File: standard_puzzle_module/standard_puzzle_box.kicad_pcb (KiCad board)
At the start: 2 copper layers, 76 parts, among them U1 ESP32-C3-DevKitM-1

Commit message: feat: salvaging stuff after lossy crash
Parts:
- R_BO1, R_BO2, R_BO3, R_BO4, R_BO5, R_BO6, R_SIN1, R_SIN2, R_SIN3, R_SIN4, R_SO1, R_SO10, R_SO2, R_SO3, R_SO4, R_SO5, R_SO6, R_SO7, R_SO8, R_SO9: footprint Resistor_THT:R_Axial_DIN0411_L9.9mm_D3.6mm_P15.24mm_Horizontal -> Resistor_THT:R_Axial_DIN0207_L6.3mm_D2.5mm_P10.16mm_Horizontal
- U1: value ESP32-C3-DevKitM-1 -> ESP32-C3-SuperMini; footprint RF_Module:ESP32-C3-DevKitM-1 -> ESP32-C3-SuperMini:ESP32-C3-SuperMini
- moved R_BO6 204.4 mm to (106.4, 87.4)
- moved J_BI4 197.0 mm to (172.0, 32.2), turned to 180 degrees
- moved J_BI3 190.6 mm to (188.6, 31.8), turned to 180 degrees
- moved CP_BO2 188.4 mm to (153.9, 106.0)
- moved R_BO4 187.1 mm to (139.2, 86.6)
- moved R_BO5 184.8 mm to (131.7, 93.8), turned to -90 degrees
- moved D_BO2 183.9 mm to (153.8, 98.5), turned to 180 degrees
- moved J_BO2 183.1 mm to (146.9, 106.0), turned to 180 degrees
- moved CP_BO1 181.5 mm to (184.1, 105.7)
- moved U_BO2 181.4 mm to (165.2, 88.6), turned to 180 degrees
- moved Q_BO2 179.6 mm to (146.2, 91.5), turned to 180 degrees
- moved D_BI3 179.6 mm to (191.0, 50.1), turned to 180 degrees
- moved D_BI4 179.5 mm to (177.5, 50.1), turned to 180 degrees
- moved U_BI4 177.8 mm to (174.0, 56.6), turned to 180 degrees
- moved CC_BO2 177.5 mm to (158.8, 92.9), turned to 180 degrees
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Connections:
- CC_PI1 pad 1: Net-(DCREG1-Vin) -> +12V
- CP_PI1 pad 1: Net-(DCREG1-Vin) -> +12V
- DCREG1 pad 1: Net-(DCREG1-Vin) -> +12V
- D_SCHP1 pad 1: Net-(DCREG1-Vin) -> +12V
- FUSE1 pad 1: +12V -> Net-(J_PWR1-Pin_1)
- J_PWR1 pad 1: +12V -> Net-(J_PWR1-Pin_1)
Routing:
- net +12V: track 8.02 -> 97.5 mm
- net GND: track 57.0 -> 93.4 mm, vias 8 -> 14
- net +5V: track 43.5 -> 10.6 mm
- net +3.3V: track 29.4 -> 0.00 mm, vias 0 -> 1
- net Net-(DCREG1-Vin): track 19.7 -> 0.00 mm
- net Net-(D_BO3-A): track 0.00 -> 15.9 mm
- net Net-(D_BO1-A): track 0.00 -> 15.9 mm
- net Net-(D_BO2-A): track 0.00 -> 15.2 mm
- net Net-(Q_BO3-G): track 0.00 -> 14.2 mm
- net Net-(Q_BO2-G): track 0.00 -> 13.7 mm
- net Net-(R_BO5-Pad1): track 0.00 -> 13.7 mm, vias 0 -> 2
- net /signal_input/out: track 13.3 -> 0.00 mm
- net Net-(R_BO3-Pad1): track 0.00 -> 11.9 mm, vias 0 -> 2
- net Net-(Q_BO1-G): track 0.00 -> 11.7 mm
- net Net-(R_BO1-Pad1): track 0.00 -> 11.6 mm, vias 0 -> 2
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
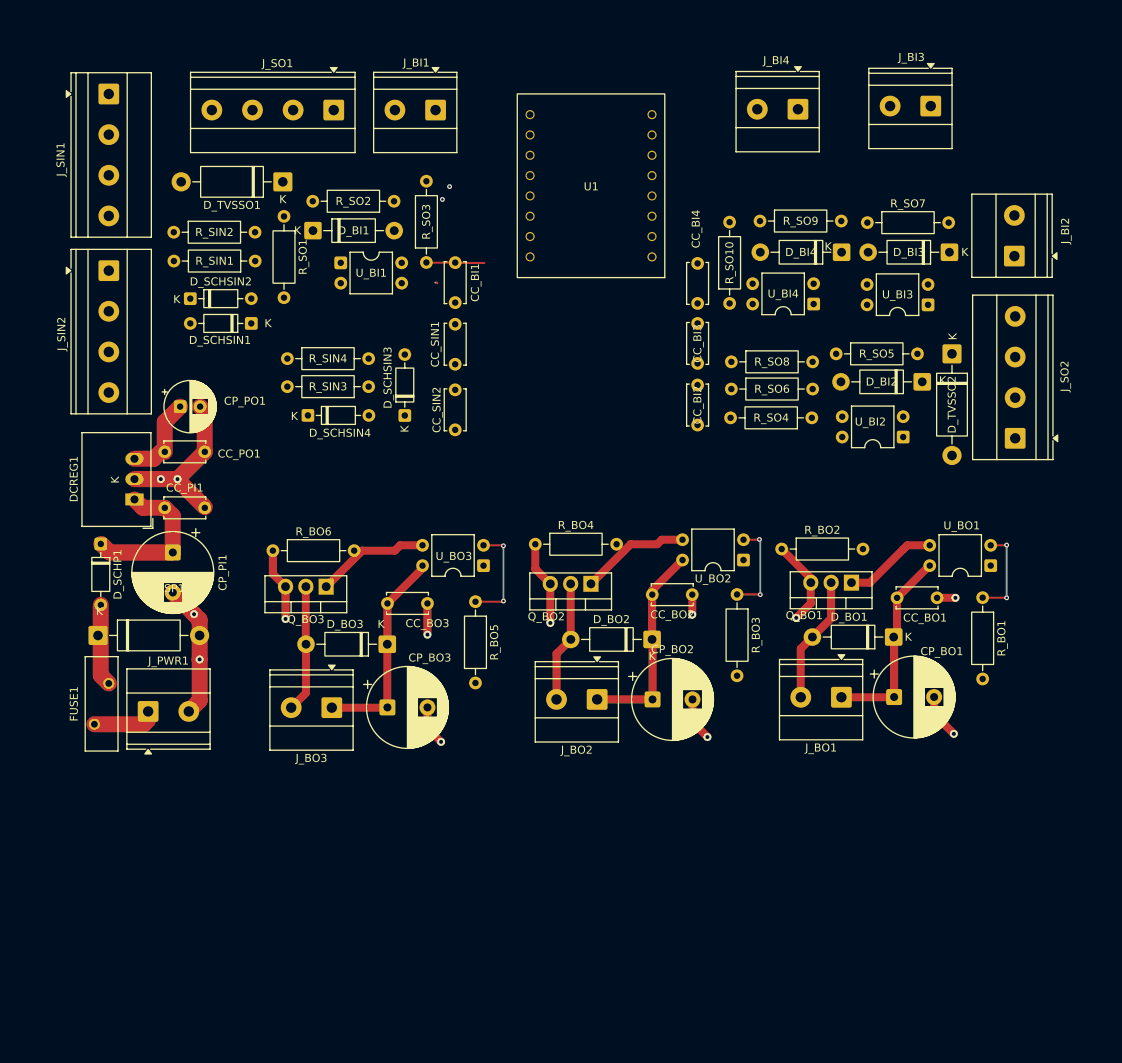
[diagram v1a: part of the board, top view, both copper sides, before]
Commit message: feat: improve component placement for pcb
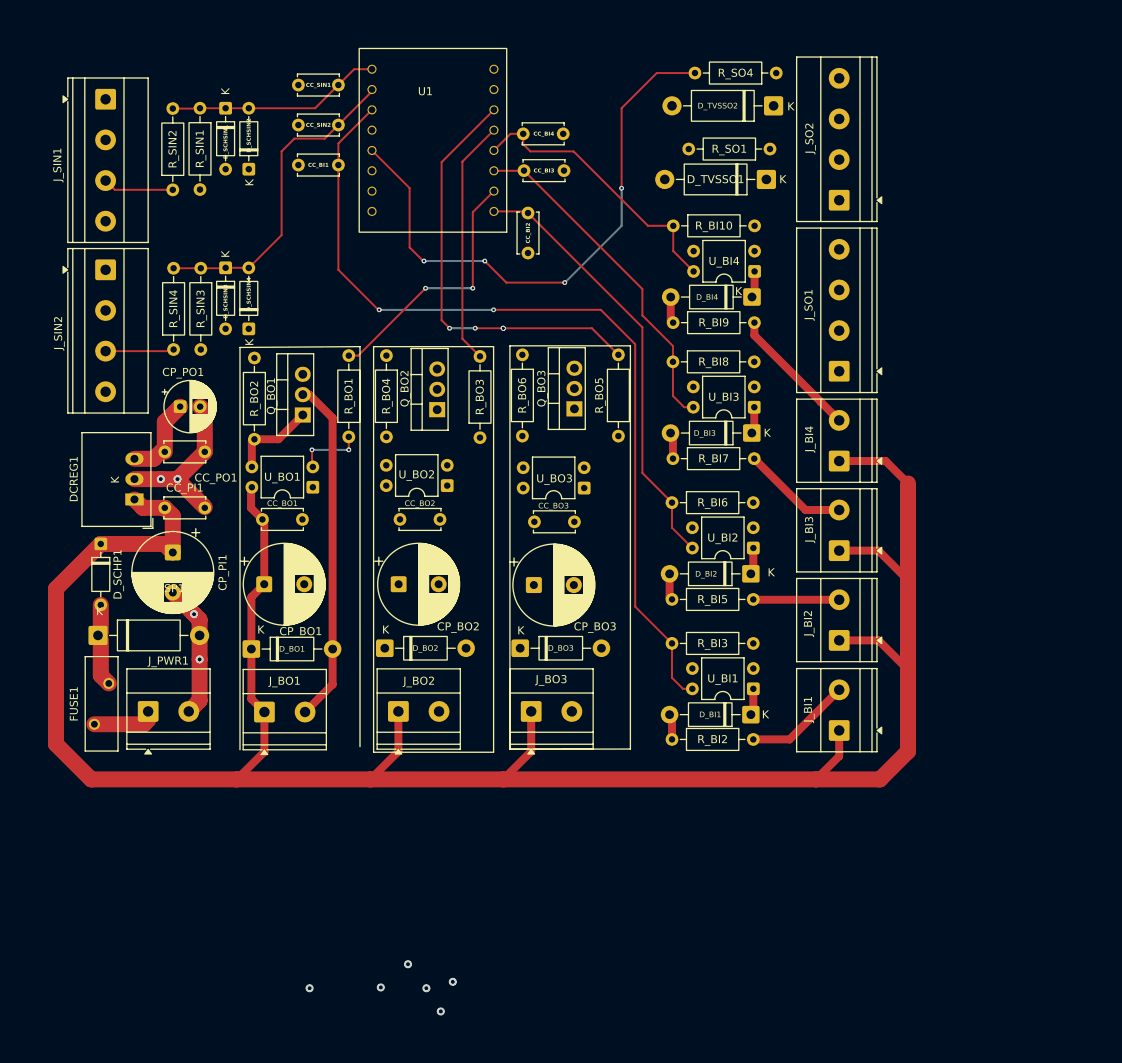
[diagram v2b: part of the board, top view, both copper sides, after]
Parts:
- moved J_BI1 92.5 mm to (177.2, 109.9), turned to 90 degrees
- moved U_BO1 85.3 mm to (111.4, 79.5)
- moved R_BO1 81.7 mm to (115.9, 73.2), turned to 90 degrees
- moved D_BI1 81.6 mm to (166.2, 107.9), turned to 180 degrees
- moved D_BO1 80.3 mm to (103.7, 99.7), turned to 0 degrees
- moved CP_BO1 80.0 mm to (105.3, 91.6)
- moved CC_BO1 79.9 mm to (110.1, 83.5)
- moved R_BI2 75.7 mm to (156.3, 111.0), turned to 0 degrees
- moved U_BI1 74.1 mm to (166.5, 104.7), turned to 180 degrees
- moved J_BO1 72.1 mm to (105.4, 107.6), turned to 0 degrees
- moved Q_BO1 71.7 mm to (110.2, 70.4), turned to 90 degrees
- moved J_SO1 71.1 mm to (177.2, 65.0), turned to 90 degrees
- moved R_BO2 70.1 mm to (104.1, 63.3), turned to -90 degrees
- moved R_SO1 61.3 mm to (168.6, 37.2), turned to 180 degrees
- moved D_TVSSO1 60.5 mm to (168.1, 41.0)
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- renumbered R_SO10 to R_BI10, R_SO2 to R_BI2, R_SO3 to R_BI3, R_SO5 to R_BI5, R_SO6 to R_BI6, R_SO7 to R_BI7, R_SO8 to R_BI8, R_SO9 to R_BI9
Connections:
- U1 pad 0: GND -> /signal_input/out
- U1 pad 1: GND -> /signal_input1/out
- U1 pad 10: /signal_input1/out -> /boolean_output2/in
- U1 pad 2: +3.3V -> /boolean_input/out
- U1 pad 20: /signal_output1/in -> unconnected-(U1-GPIO20-Pad20)
- U1 pad 21: /boolean_input1/out -> unconnected-(U1-GPIO21-Pad21)
- U1 pad 3: +3.3V -> /signal_output/in
- U1 pad 3V3: +5V -> (no net)
- U1 pad 4: /boolean_input/out -> /signal_output1/in
- U1 pad 5: /signal_output/in -> /boolean_input1/out
- U1 pad 5V: +5V -> (no net)
- U1 pad 6: GND -> /boolean_output/in
- U1 pad 7: unconnected-(U1-RST-Pad7) -> /boolean_input2/out
- U1 pad 8: GND -> /boolean_input3/out
- U1 pad 9: /signal_input/out -> /boolean_output1/in
- U1 pad GND: /boolean_output2/in -> (no net)
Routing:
- net +12V: track 97.5 -> 287.7 mm
- net /boolean_input/out: track 7.26 -> 109.3 mm, vias 0 -> 2
- net /signal_output1/in: track 0.00 -> 71.0 mm, vias 0 -> 4
- net GND: track 93.4 -> 38.2 mm, vias 14 -> 10
- net /boolean_input1/out: track 0.00 -> 54.7 mm
- net /boolean_output2/in: track 0.00 -> 53.0 mm, vias 0 -> 6
- net /boolean_input2/out: track 0.00 -> 42.8 mm
- net /signal_input1/out: track 0.00 -> 40.3 mm
- net /boolean_input3/out: track 0.00 -> 35.6 mm
- net /boolean_output/in: track 0.00 -> 32.1 mm, vias 0 -> 2
- net /boolean_output1/in: track 0.00 -> 30.8 mm
- net Net-(D_BO1-A): track 15.9 -> 43.1 mm
- net /signal_input/out: track 0.00 -> 26.9 mm
- net Net-(J_BI4-Pin_2): track 0.00 -> 16.6 mm
- net Net-(D_BO3-A): track 15.9 -> 0.00 mm
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
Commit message: feat: DRC approved prototype of the board
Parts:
- moved CC_BO3 33.4 mm to (110.7, 84.8)
- moved CP_BO3 33.4 mm to (105.6, 91.9)
- moved D_BO3 33.4 mm to (103.9, 99.8)
- moved J_BO3 33.4 mm to (105.3, 107.7)
- moved Q_BO3 33.4 mm to (110.7, 69.9)
- moved R_BO5 33.4 mm to (116.2, 73.3)
- moved U_BO3 33.4 mm to (111.9, 79.8)
- moved R_BO6 33.3 mm to (104.3, 63.1)
- moved J_BO1 30.6 mm to (136.0, 107.7)
- moved CP_BO1 30.6 mm to (135.9, 91.7)
- moved U_BO1 30.6 mm to (142.0, 79.6)
- moved CC_BO1 30.6 mm to (140.7, 83.6)
- moved D_BO1 30.6 mm to (134.3, 99.8)
- moved Q_BO1 30.6 mm to (140.8, 70.5)
- moved R_BO1 30.6 mm to (146.5, 73.3)
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- renumbered D_SCHSIN1 to DS_SI1, D_SCHSIN2 to DS_SI2, D_SCHSIN3 to DS_SI3, D_SCHSIN4 to DS_SI4
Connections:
- U1 pad 3V3: (no net) -> +3.3V
- U1 pad 5V: (no net) -> +5V
- U1 pad GND: (no net) -> GND
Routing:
- net +3.3V: track 0.00 -> 289.4 mm, vias 0 -> 23
- net +5V: track 10.6 -> 224.4 mm
- net /signal_output/in: track 0.00 -> 67.2 mm, vias 0 -> 2
- net +12V: track 287.7 -> 349.0 mm
- net Net-(D_BO3-A): track 0.00 -> 46.8 mm
- net Net-(D_BO2-A): track 0.00 -> 46.6 mm
- net Net-(D_TVSSO1-K): track 0.00 -> 25.9 mm, vias 0 -> 2
- net Net-(D_TVSSO2-K): track 0.00 -> 15.0 mm
- net Net-(Q_BO3-G): track 0.00 -> 11.8 mm
- net Net-(Q_BO2-G): track 0.00 -> 11.3 mm
- net /boolean_input1/out: track 54.7 -> 64.0 mm, vias 0 -> 4
- net /boolean_output/in: track 32.1 -> 40.5 mm
- net /boolean_input2/out: track 42.8 -> 50.4 mm, vias 0 -> 4
- net Net-(R_BO5-Pad1): track 0.00 -> 7.26 mm
- net Net-(R_BO3-Pad1): track 0.00 -> 6.66 mm
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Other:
- board outline added: 112 x 95 mm

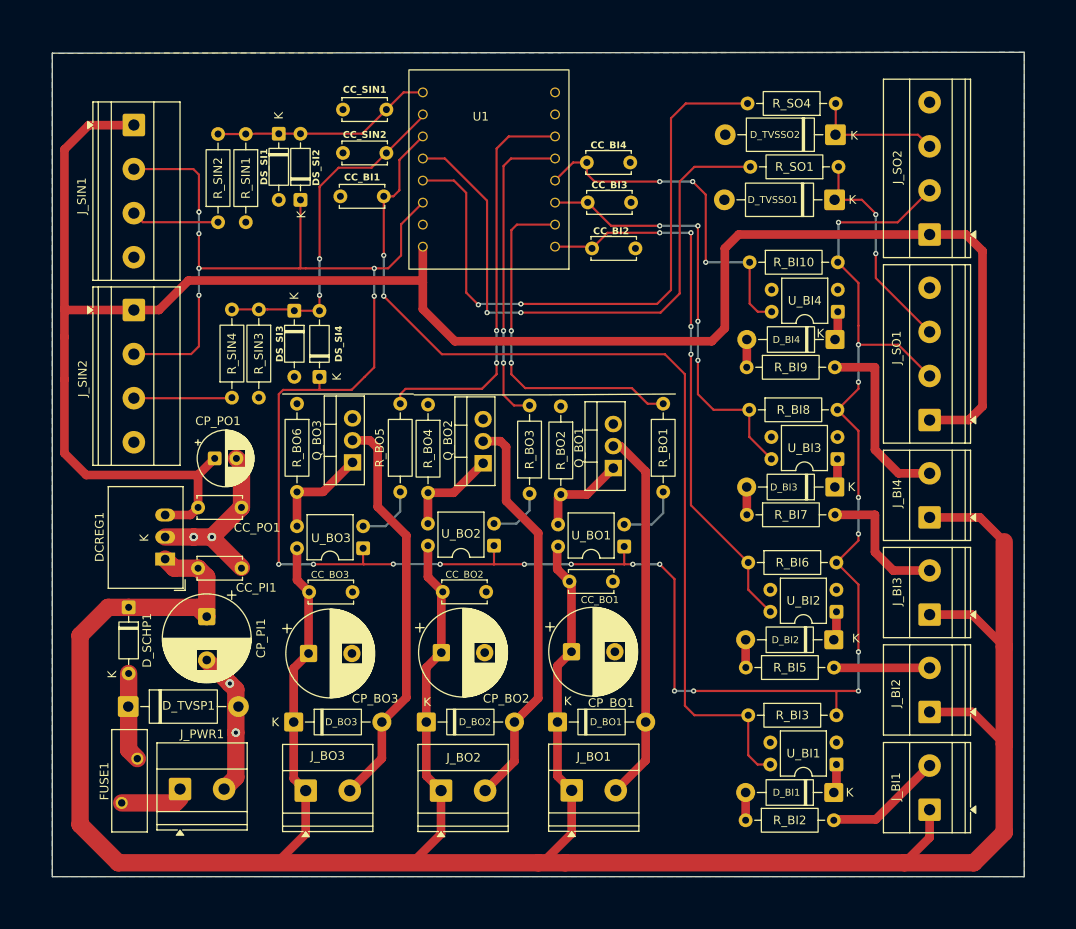
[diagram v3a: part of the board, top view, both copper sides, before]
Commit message: feat: decrease the board size
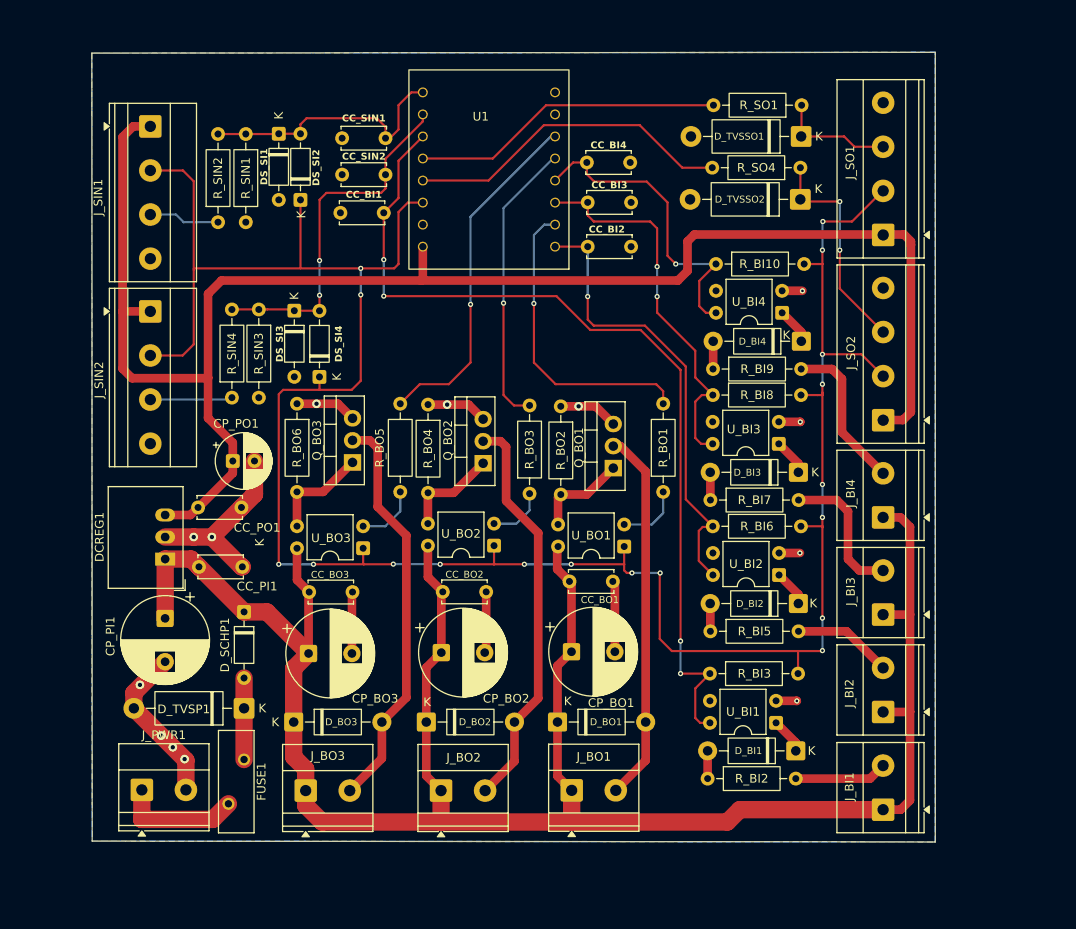
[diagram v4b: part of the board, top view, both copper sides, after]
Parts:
- moved J_SO2 22.1 mm to (171.8, 65.0)
- moved J_SO1 22.0 mm to (171.8, 43.6)
- moved D_TVSP1 13.4 mm to (98.2, 98.2), turned to 180 degrees
- moved D_SCHP1 13.3 mm to (98.2, 87.1)
- moved FUSE1 12.3 mm to (96.4, 109.2)
- moved D_TVSSO2 8.48 mm to (162.3, 39.5)
- moved U_BI1 8.45 mm to (159.5, 99.9)
- moved R_SO4 8.45 mm to (162.3, 35.9)
- moved R_SO1 8.27 mm to (162.4, 28.7)
- moved D_TVSSO1 8.25 mm to (162.4, 32.3)
- moved U_BI2 7.85 mm to (159.8, 82.8)
- moved U_BI3 6.99 mm to (159.8, 67.7)
- moved R_BI3 6.53 mm to (151.9, 94.2)
- moved D_BI1 6.50 mm to (161.8, 103.1)
- moved R_BI2 6.50 mm to (151.6, 106.3)
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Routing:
- net +12V: track 349.0 -> 240.0 mm
- net GND: track 38.2 -> 92.9 mm, vias 4 -> 16
- net +5V: track 224.4 -> 189.5 mm
- net /signal_output1/in: track 71.3 -> 38.0 mm, vias 2 -> 0
- net /signal_output/in: track 67.2 -> 36.0 mm, vias 2 -> 0
- net +3.3V: track 289.4 -> 269.9 mm, vias 23 -> 18
- net Net-(D_TVSSO1-K): track 25.9 -> 13.6 mm, vias 2 -> 0
- net /boolean_input1/out: track 64.0 -> 53.0 mm, vias 4 -> 1
- net Net-(D_TVSSO2-K): track 15.0 -> 25.5 mm, vias 0 -> 2
- net /boolean_input/out: track 112.9 -> 104.2 mm, vias 2 -> 4
- net Net-(J_PWR1-Pin_1): track 8.02 -> 14.2 mm
- net /boolean_output2/in: track 46.5 -> 40.4 mm, vias 2 -> 1
- net /boolean_input2/out: track 50.4 -> 44.6 mm, vias 4 -> 2
- net /signal_input/out: track 24.8 -> 30.5 mm
- net /boolean_output/in: track 40.5 -> 35.3 mm, vias 2 -> 1
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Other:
- board size 112 x 95 mm -> 97.2 x 91 mm

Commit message: feat: generate gerber files
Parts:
- added REF**: OSHW-Logo2_9.8x8mm_SilkScreen, Symbol:OSHW-Logo2_9.8x8mm_SilkScreen, B.Cu at (143.4, 56.9)
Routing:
- net +5V: track 189.5 -> 188.8 mm
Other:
- board text added: "Licensed under CC-BY-SA 4.0"
- board text added: "Universal Puzzle Node www.github.com/Nattotata/schematics for unIQue room by David Seidler reldies.divad@gmail.com on 28.08.2026"
